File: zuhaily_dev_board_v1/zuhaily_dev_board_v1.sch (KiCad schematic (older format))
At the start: 43 parts

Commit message: branch commit
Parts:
- added U?: 4001, symbol 4xxx_IEEE:4001
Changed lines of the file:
@@
+	1    0    0    -1
+$EndComp
+$Comp
+L 4xxx_IEEE:4001 U?
+U 1 1 5C5155E3
+P 17750 2550
+F 0 "U?" H 18291 2609 50  0000 L CNN
+F 1 "4001" H 18291 2518 50  0000 L CNN
+F 2 "" H 17750 2550 50  0001 C CNN
+F 3 "" H 17750 2550 50  0001 C CNN
+	1    17750 2550
 	1    0    0    -1
 $EndComp

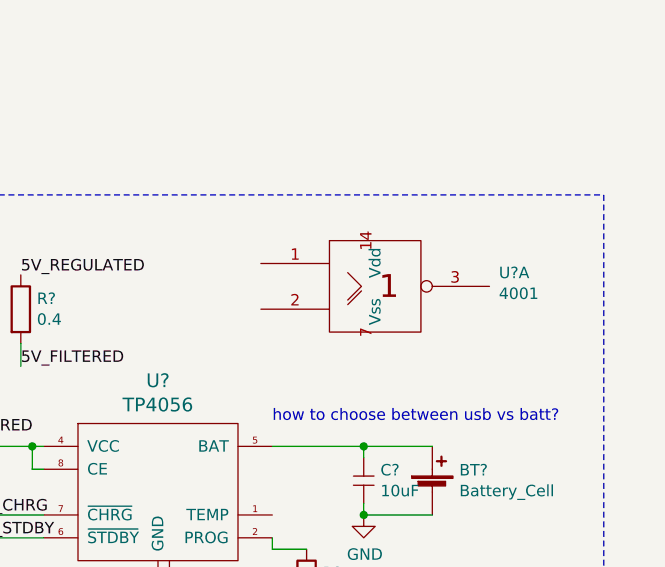
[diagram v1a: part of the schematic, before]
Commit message: removed test branch changes
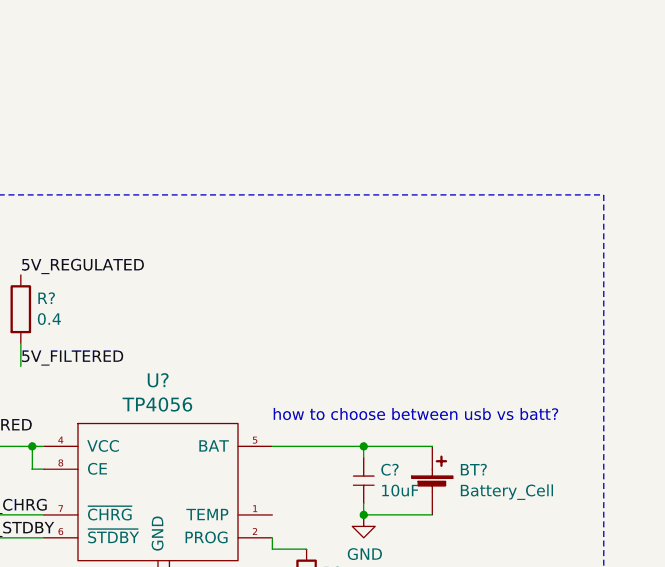
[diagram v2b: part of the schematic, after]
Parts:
- removed U?: 4001, symbol 4xxx_IEEE:4001
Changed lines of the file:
@@
-	1    0    0    -1
-$EndComp
-$Comp
-L 4xxx_IEEE:4001 U?
-U 1 1 5C5155E3
-P 17750 2550
-F 0 "U?" H 18291 2609 50  0000 L CNN
-F 1 "4001" H 18291 2518 50  0000 L CNN
-F 2 "" H 17750 2550 50  0001 C CNN
-F 3 "" H 17750 2550 50  0001 C CNN
-	1    17750 2550
 	1    0    0    -1
 $EndComp
